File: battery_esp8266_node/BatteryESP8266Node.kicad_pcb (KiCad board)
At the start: 2 copper layers, 22.9 x 26.7 mm, 16 parts, among them J1 Power, J2 UART, SW1 Reset, SW2 Flash, U1 ESP-12E, U2 AP2112K-3.3

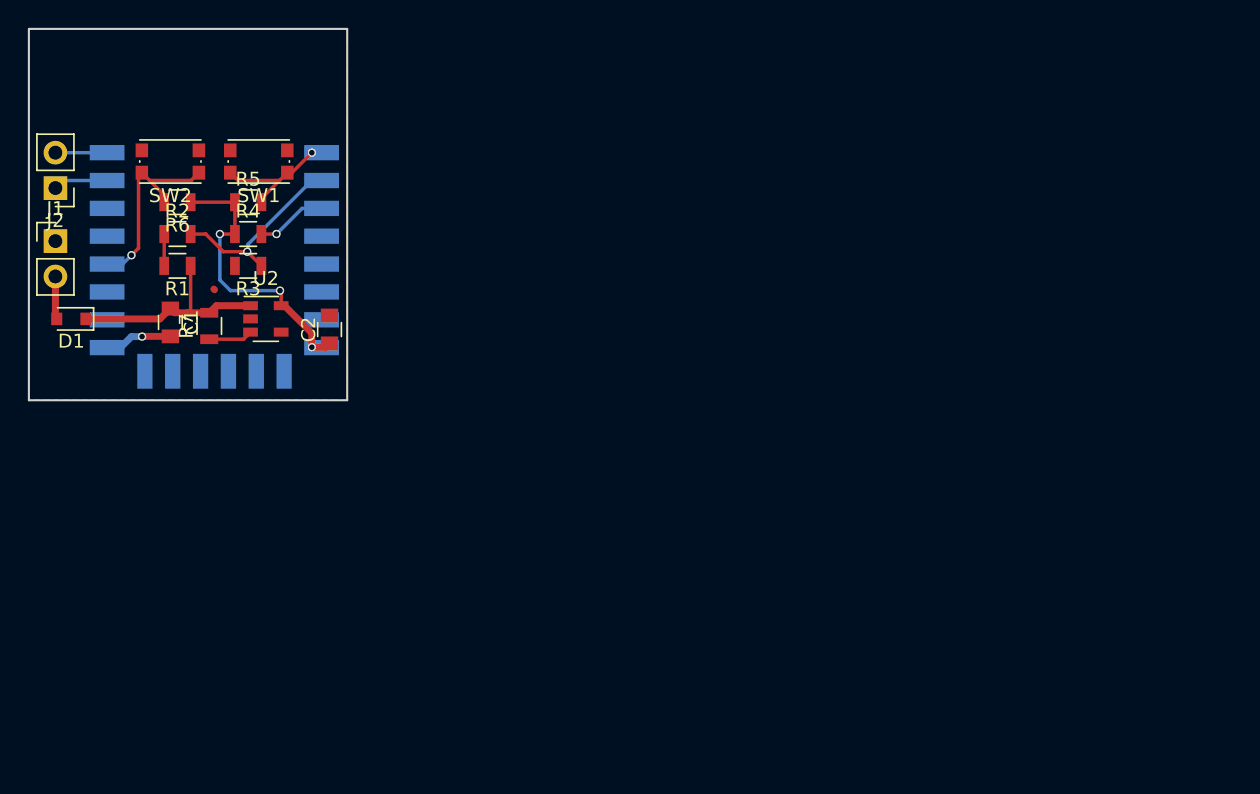
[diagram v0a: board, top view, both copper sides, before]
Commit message: Second board revision
All components on a single side, generally neater layout, added proto
headers.
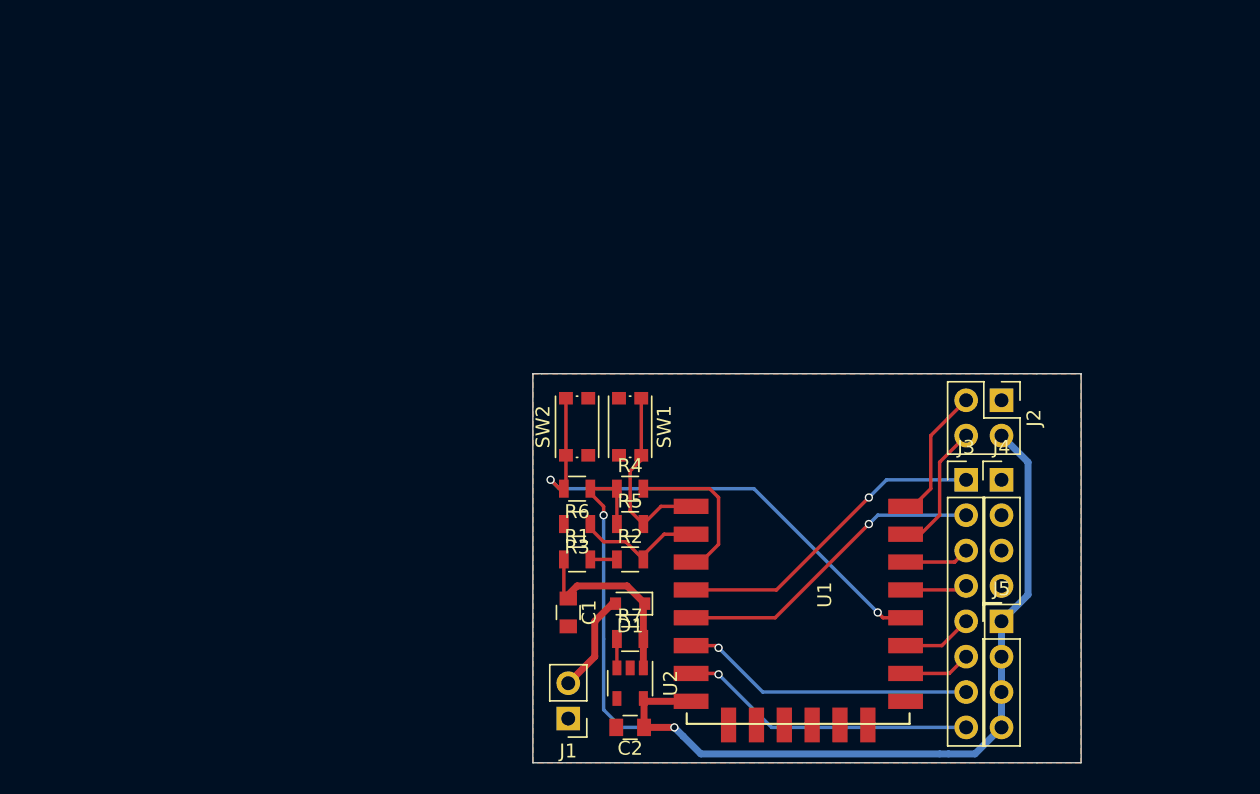
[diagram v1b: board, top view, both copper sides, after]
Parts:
- added J3: IO, Pin_Headers:Pin_Header_Straight_1x08_Pitch2.54mm, F.Cu at (181.6, 97.2)
- added J4: GND, Pin_Headers:Pin_Header_Straight_1x04_Pitch2.54mm, F.Cu at (184.2, 97.2)
- added J5: 3V3, Pin_Headers:Pin_Header_Straight_1x04_Pitch2.54mm, F.Cu at (184.2, 107.3)
- J2: footprint Pin_Headers:Pin_Header_Straight_1x02_Pitch2.54mm -> Pin_Headers:Pin_Header_Straight_2x02_Pitch2.54mm
- U1: moved to F.Cu
- moved J2 69.6 mm to (184.2, 91.4), turned to 270 degrees
- moved J1 50.3 mm to (153.0, 114.3), turned to 180 degrees
- moved D1 45.0 mm to (157.5, 106.0)
- moved R2 40.0 mm to (157.5, 102.9)
- moved U1 37.8 mm to (162.6, 99.1), turned to 0 degrees
- moved R7 37.7 mm to (157.5, 108.6), turned to 0 degrees
- moved U2 37.0 mm to (157.5, 111.8), turned to 270 degrees
- moved R5 35.9 mm to (157.5, 100.3)
- moved C2 35.8 mm to (157.5, 114.9), turned to 180 degrees
- moved R1 35.6 mm to (153.7, 102.9), turned to 0 degrees
- moved C1 35.4 mm to (153.0, 106.7)
- moved R6 35.3 mm to (153.7, 97.8)
- moved SW2 34.9 mm to (153.7, 93.3), turned to 90 degrees
- moved R4 33.0 mm to (157.5, 97.8)
- moved SW1 32.8 mm to (157.5, 93.3), turned to 270 degrees
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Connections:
- J2 pad 1: /ESP_UART_RX -> GND
- J2 pad 2: /ESP_UART_TX -> +3V3
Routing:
- net +3V3: track 21.0 -> 82.4 mm, vias 3 -> 2
- net /ESP_FLASH: track 14.1 -> 36.7 mm, vias 1 -> 2
- net /IO_16: track 0.00 -> 22.3 mm, vias 0 -> 1
- net /IO_14: track 0.00 -> 22.1 mm, vias 0 -> 1
- net /IO_13: track 0.00 -> 20.7 mm, vias 0 -> 1
- net /IO_12: track 0.00 -> 20.4 mm, vias 0 -> 1
- net /IO_5: track 0.00 -> 7.08 mm
- net /ESP_UART_TX: track 4.42 -> 11.0 mm
- net /ESP_CH_PD: track 4.77 -> 10.8 mm, vias 1 -> 0
- net /IO_2: track 0.00 -> 5.77 mm
- net /ESP_UART_RX: track 4.64 -> 10.2 mm
- net /IO_15: track 0.00 -> 5.55 mm
- net /ESP_RESET: track 9.02 -> 14.4 mm, vias 1 -> 0
- net /IO_4: track 0.00 -> 5.17 mm
- net GND: track 4.17 -> 0.00 mm, vias 1 -> 0
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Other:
- board size 22.9 x 26.7 mm -> 39.4 x 27.9 mm
- rule pad_to_mask_clearance: 0.2 -> 0

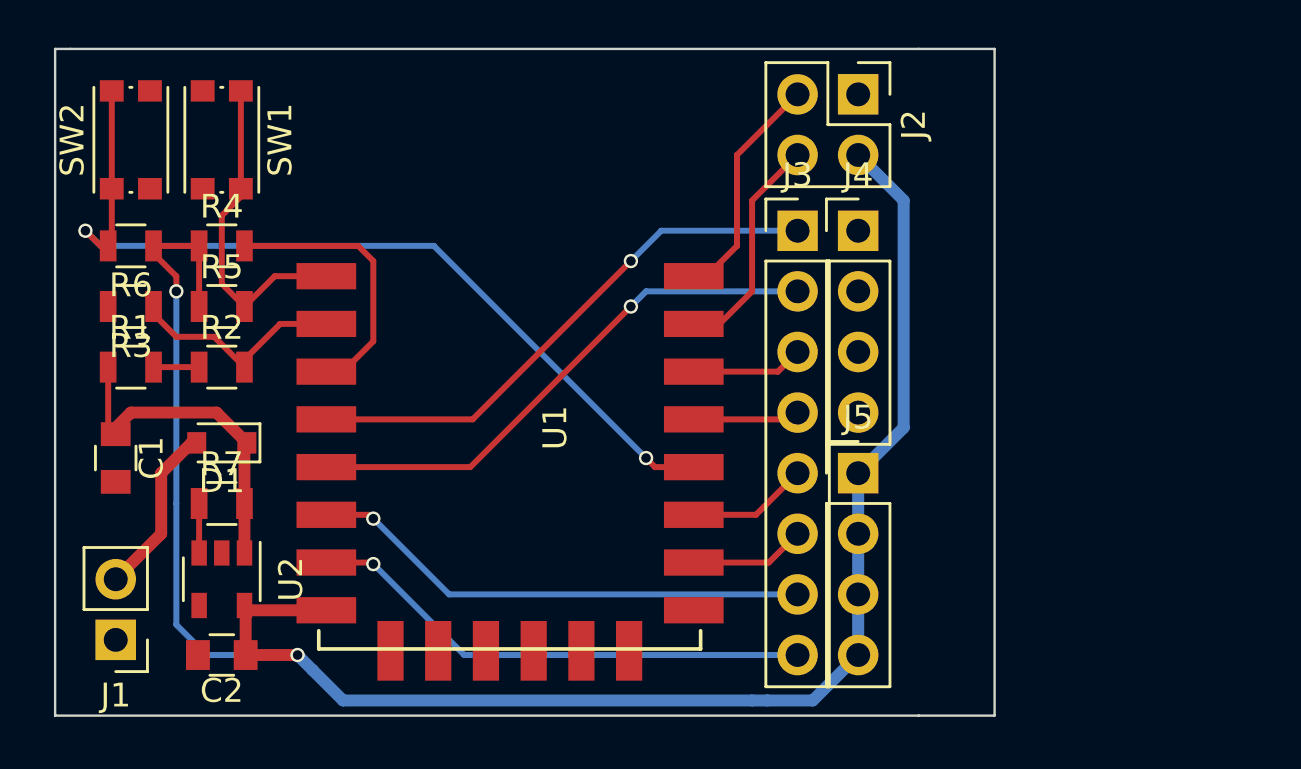
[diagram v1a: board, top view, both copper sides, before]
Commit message: Add prototyping area
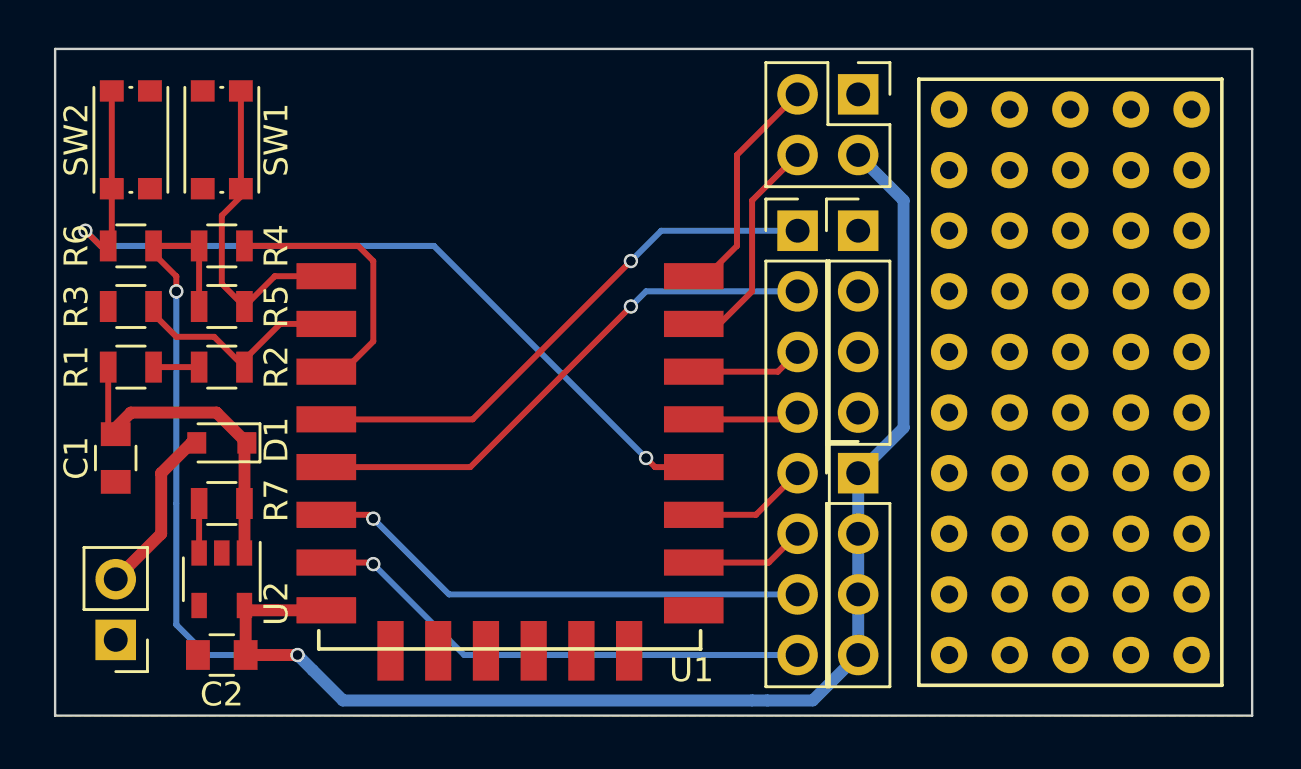
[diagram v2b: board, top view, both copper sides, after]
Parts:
- added REF**: Prototype_Area_05x10_TH_Pitch2.54mm, prototype_areas:Prototype_Area_05x10_TH_Pitch2.54mm, F.Cu at (193.0, 103.5)
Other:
- board size 39.4 x 27.9 mm -> 50.2 x 27.9 mm

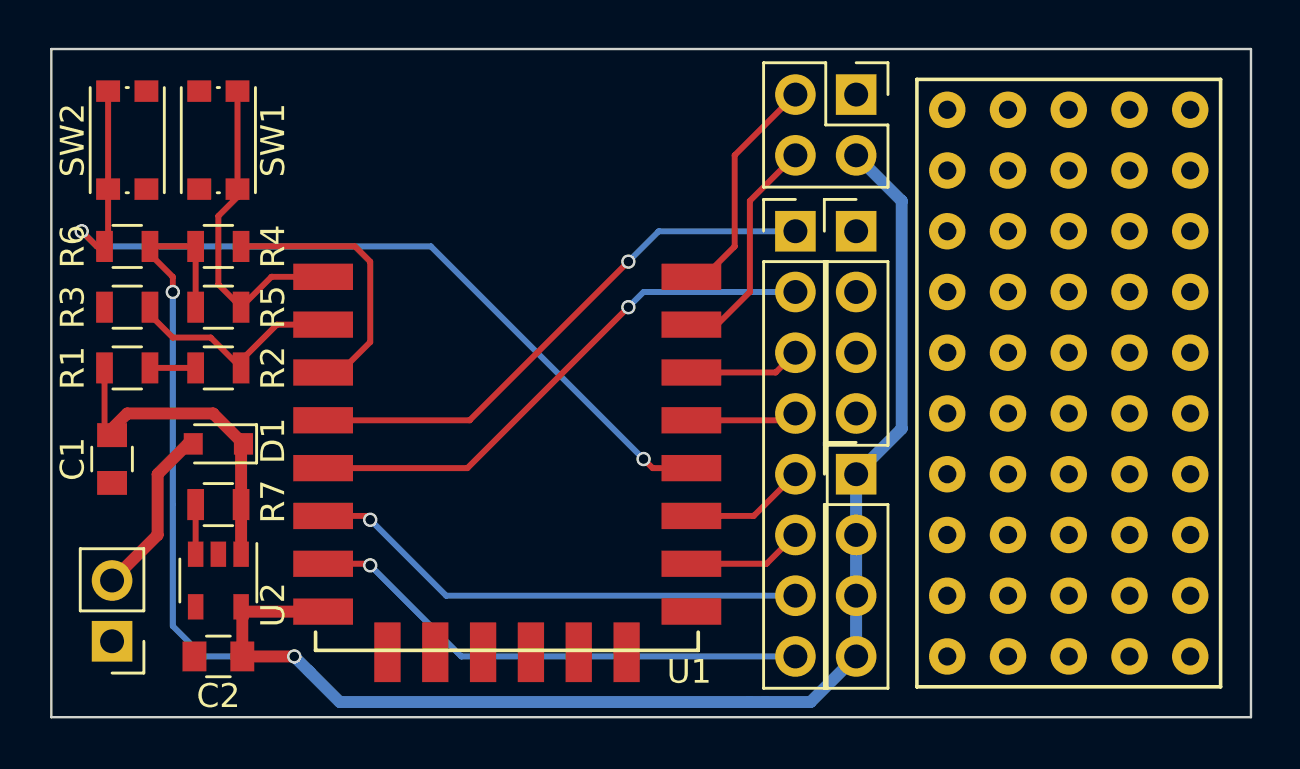
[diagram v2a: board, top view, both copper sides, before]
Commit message: Reduce board size slightly and add dimensions
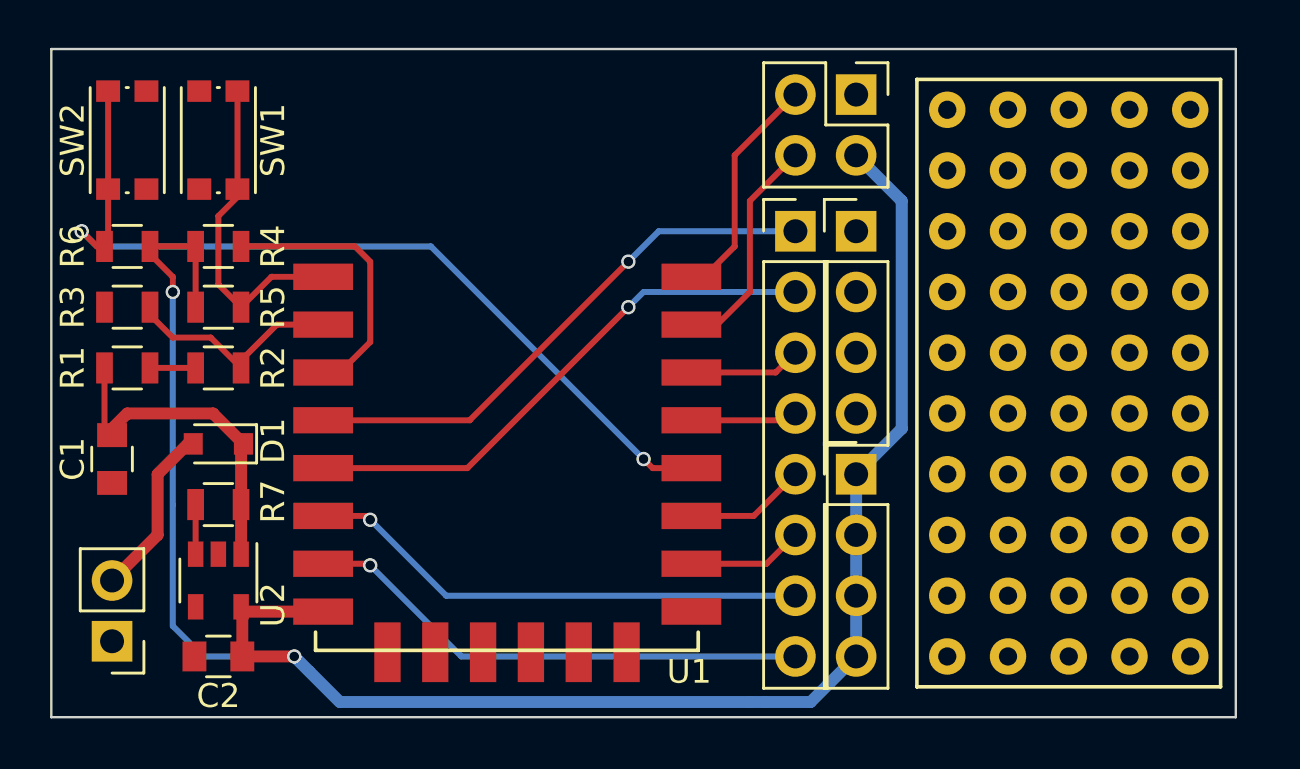
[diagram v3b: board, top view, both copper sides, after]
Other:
- board size 50.2 x 27.9 mm -> 49.5 x 27.9 mm
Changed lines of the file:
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@@
     (links 50)
     (no_connects 0)
-    (area 150.444999 89.484999 200.710001 117.525001)
+    (area 150.31 85.385 209.78 118.55)
     (thickness 1.6)
-    (drawings 4)
+    (drawings 6)
     (tracks 112)
     (zones 0)
@@
       (outputformat 1)
       (mirror false)
-      (drillshape 1)
+      (drillshape 0)
       (scaleselection 1)
       (outputdirectory ""))
@@
     (pad 50 thru_hole circle (at 5.08 11.43) (size 1.524 1.524) (drill 0.762) (layers *.Cu *.Mask))
   )
-  (gr_line (start 150.495 117.475) (end 200.66 117.475) (angle 90) (layer Edge.Cuts) (width 0.1))
-  (gr_line (start 200.66 89.535) (end 150.495 89.535) (angle 90) (layer Edge.Cuts) (width 0.1))
+  (dimension 27.94 (width 0.3) (layer Dwgs.User)
+    (gr_text "27.940 mm" (at 202.645 103.505 270) (layer Dwgs.User)
+      (effects (font (size 1.5 1.5) (thickness 0.3)))
+    )
+    (feature1 (pts (xy 200.025 117.475) (xy 203.995 117.475)))
+    (feature2 (pts (xy 200.025 89.535) (xy 203.995 89.535)))
+    (crossbar (pts (xy 201.295 89.535) (xy 201.295 117.475)))
+    (arrow1a (pts (xy 201.295 117.475) (xy 200.708579 116.348496)))
+    (arrow1b (pts (xy 201.295 117.475) (xy 201.881421 116.348496)))
+    (arrow2a (pts (xy 201.295 89.535) (xy 200.708579 90.661504)))
+    (arrow2b (pts (xy 201.295 89.535) (xy 201.881421 90.661504)))
+  )
+  (gr_line (start 150.495 89.535) (end 200.025 89.535) (angle 90) (layer Edge.Cuts) (width 0.1))
+  (gr_line (start 200.025 117.475) (end 150.495 117.475) (angle 90) (layer Edge.Cuts) (width 0.1))
+  (dimension 49.53 (width 0.3) (layer Dwgs.User)
+    (gr_text "49.530 mm" (at 175.26 86.915) (layer Dwgs.User)
+      (effects (font (size 1.5 1.5) (thickness 0.3)))
+    )
+    (feature1 (pts (xy 150.495 89.535) (xy 150.495 85.565)))
+    (feature2 (pts (xy 200.025 89.535) (xy 200.025 85.565)))
+    (crossbar (pts (xy 200.025 88.265) (xy 150.495 88.265)))
+    (arrow1a (pts (xy 150.495 88.265) (xy 151.621504 87.678579)))
+    (arrow1b (pts (xy 150.495 88.265) (xy 151.621504 88.851421)))
+    (arrow2a (pts (xy 200.025 88.265) (xy 198.898496 87.678579)))
+    (arrow2b (pts (xy 200.025 88.265) (xy 198.898496 88.851421)))
+  )
   (gr_line (start 150.495 117.475) (end 150.495 89.535) (angle 90) (layer Edge.Cuts) (width 0.1))
-  (gr_line (start 200.66 89.535) (end 200.66 117.475) (angle 90) (layer Edge.Cuts) (width 0.1))
+  (gr_line (start 200.025 89.535) (end 200.025 117.475) (angle 90) (layer Edge.Cuts) (width 0.1))
   (segment (start 152.72 102.87) (end 152.72 105.365) (width 0.25) (layer F.Cu) (net 1))
   (segment (start 152.72 105.365) (end 153.035 105.68) (width 0.25) (layer F.Cu) (net 1))
@@
     (polygon
       (pts
-        (xy 200.66 117.475) (xy 150.495 117.475) (xy 150.495 89.535) (xy 200.66 89.535)
+        (xy 200.025 117.475) (xy 150.495 117.475) (xy 150.495 89.535) (xy 200.025 89.535)
       )
     )

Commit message: Add silkscreen, final check
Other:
- board text added: "12"
- board text added: "13"
- board text added: "14"
- board text added: "15"
- board text added: "16"
- board text added: "2"
- board text added: "3V3"
- board text added: "4"
- board text added: "5"
- board text added: "Bare ESP8266 Node dan-nixon.com"
- board text added: "FLASH"
- board text added: "GND"
- board text added: "RESET"
- board text added: "RX"
- board text added: "TX"
- board text added: "VIN"
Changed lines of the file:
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@@
     (links 50)
     (no_connects 0)
-    (area 150.31 85.385 209.78 118.55)
+    (area 150.31 85.385 209.145 118.55)
     (thickness 1.6)
-    (drawings 6)
+    (drawings 31)
     (tracks 112)
     (zones 0)
@@
     (visible_elements FFFFFF7F)
     (pcbplotparams
-      (layerselection 0x00030_80000001)
+      (layerselection 0x010f0_80000001)
       (usegerberextensions false)
       (excludeedgelayer true)
@@
       (drillshape 0)
       (scaleselection 1)
-      (outputdirectory ""))
+      (outputdirectory g/))
   )
   (net 0 "")
@@
     (tags "tactile switch kmr2")
     (attr smd)
-    (fp_text reference SW1 (at 0 -2.286 270) (layer F.SilkS)
+    (fp_text reference SW1 (at 0 -2.286 270) (layer F.SilkS) hide
       (effects (font (size 1 1) (thickness 0.15)))
     )
@@
     (tags "tactile switch kmr2")
     (attr smd)
-    (fp_text reference SW2 (at 0 -2.286 90) (layer F.SilkS)
+    (fp_text reference SW2 (at 0 -2.286 90) (layer F.SilkS) hide
       (effects (font (size 1 1) (thickness 0.15)))
     )
@@
     (pad 50 thru_hole circle (at 5.08 11.43) (size 1.524 1.524) (drill 0.762) (layers *.Cu *.Mask))
   )
+  (gr_text GND (at 151.13 114.3 270) (layer F.SilkS)
+    (effects (font (size 0.5 0.5) (thickness 0.1)))
+  )
+  (gr_text VIN (at 151.13 111.76 270) (layer F.SilkS)
+    (effects (font (size 0.5 0.5) (thickness 0.1)))
+  )
+  (gr_text 13 (at 179.578 114.935 90) (layer F.SilkS)
+    (effects (font (size 0.5 0.5) (thickness 0.1)))
+  )
+  (gr_text 12 (at 179.578 112.395 90) (layer F.SilkS)
+    (effects (font (size 0.5 0.5) (thickness 0.1)))
+  )
+  (gr_text 15 (at 179.578 109.855 90) (layer F.SilkS)
+    (effects (font (size 0.5 0.5) (thickness 0.1)))
+  )
+  (gr_text 2 (at 179.578 107.315 90) (layer F.SilkS)
+    (effects (font (size 0.5 0.5) (thickness 0.1)))
+  )
+  (gr_text 4 (at 179.578 104.775 90) (layer F.SilkS)
+    (effects (font (size 0.5 0.5) (thickness 0.1)))
+  )
+  (gr_text 5 (at 179.578 102.235 90) (layer F.SilkS)
+    (effects (font (size 0.5 0.5) (thickness 0.1)))
+  )
+  (gr_text 14 (at 179.578 99.695 90) (layer F.SilkS)
+    (effects (font (size 0.5 0.5) (thickness 0.1)))
+  )
+  (gr_text 16 (at 179.578 97.155 90) (layer F.SilkS)
+    (effects (font (size 0.5 0.5) (thickness 0.1)))
+  )
+  (gr_text GND (at 186.182 104.775 90) (layer F.SilkS)
+    (effects (font (size 0.5 0.5) (thickness 0.1)))
+  )
+  (gr_text GND (at 186.182 102.235 90) (layer F.SilkS)
+    (effects (font (size 0.5 0.5) (thickness 0.1)))
+  )
+  (gr_text GND (at 186.182 99.695 90) (layer F.SilkS)
+    (effects (font (size 0.5 0.5) (thickness 0.1)))
+  )
+  (gr_text GND (at 186.182 97.155 90) (layer F.SilkS)
+    (effects (font (size 0.5 0.5) (thickness 0.1)))
+  )
+  (gr_text 3V3 (at 186.182 114.935 90) (layer F.SilkS)
+    (effects (font (size 0.5 0.5) (thickness 0.1)))
+  )
+  (gr_text 3V3 (at 186.182 112.395 90) (layer F.SilkS)
+    (effects (font (size 0.5 0.5) (thickness 0.1)))
+  )
+  (gr_text 3V3 (at 186.182 109.855 90) (layer F.SilkS)
+    (effects (font (size 0.5 0.5) (thickness 0.1)))
+  )
+  (gr_text 3V3 (at 186.182 107.315 90) (layer F.SilkS)
+    (effects (font (size 0.5 0.5) (thickness 0.1)))
+  )
+  (gr_text 3V3 (at 186.182 93.98 90) (layer F.SilkS)
+    (effects (font (size 0.5 0.5) (thickness 0.1)))
+  )
+  (gr_text GND (at 186.182 91.44 90) (layer F.SilkS)
+    (effects (font (size 0.5 0.5) (thickness 0.1)))
+  )
+  (gr_text TX (at 179.578 91.44 90) (layer F.SilkS)
+    (effects (font (size 0.5 0.5) (thickness 0.1)))
+  )
+  (gr_text RX (at 179.578 93.98 90) (layer F.SilkS)
+    (effects (font (size 0.5 0.5) (thickness 0.1)))
+  )
+  (gr_text "Bare ESP8266 Node\ndan-nixon.com" (at 169.545 102.87 90) (layer B.SilkS)
+    (effects (font (size 1.5 1.5) (thickness 0.3)) (justify mirror))
+  )
+  (gr_text FLASH (at 153.67 90.17 180) (layer F.SilkS)
+    (effects (font (size 0.6 0.6) (thickness 0.1)))
+  )
+  (gr_text RESET (at 157.48 90.17 180) (layer F.SilkS)
+    (effects (font (size 0.6 0.6) (thickness 0.1)))
+  )
   (dimension 27.94 (width 0.3) (layer Dwgs.User)
